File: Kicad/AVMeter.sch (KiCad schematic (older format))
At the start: 62 parts, among them J1 Conn_01x16, J2 Screw_Terminal_01x02, J3 Screw_Terminal_01x02, J4 Screw_Terminal_01x02, J5 Screw_Terminal_01x02, J6 Conn_02x03_Odd_Even, J7 Conn_01x02, J8 Conn_01x02, U1 LT6105, U2 LT6105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

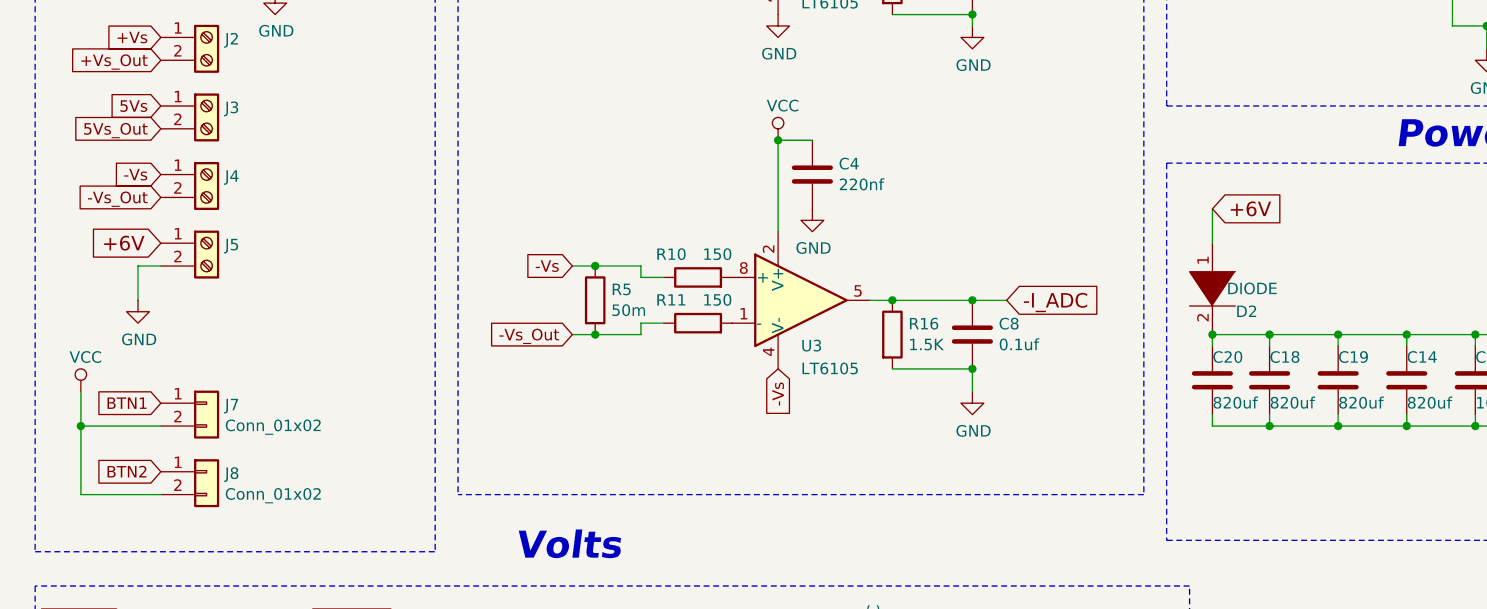
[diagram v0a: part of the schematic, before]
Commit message: fix for LM6105
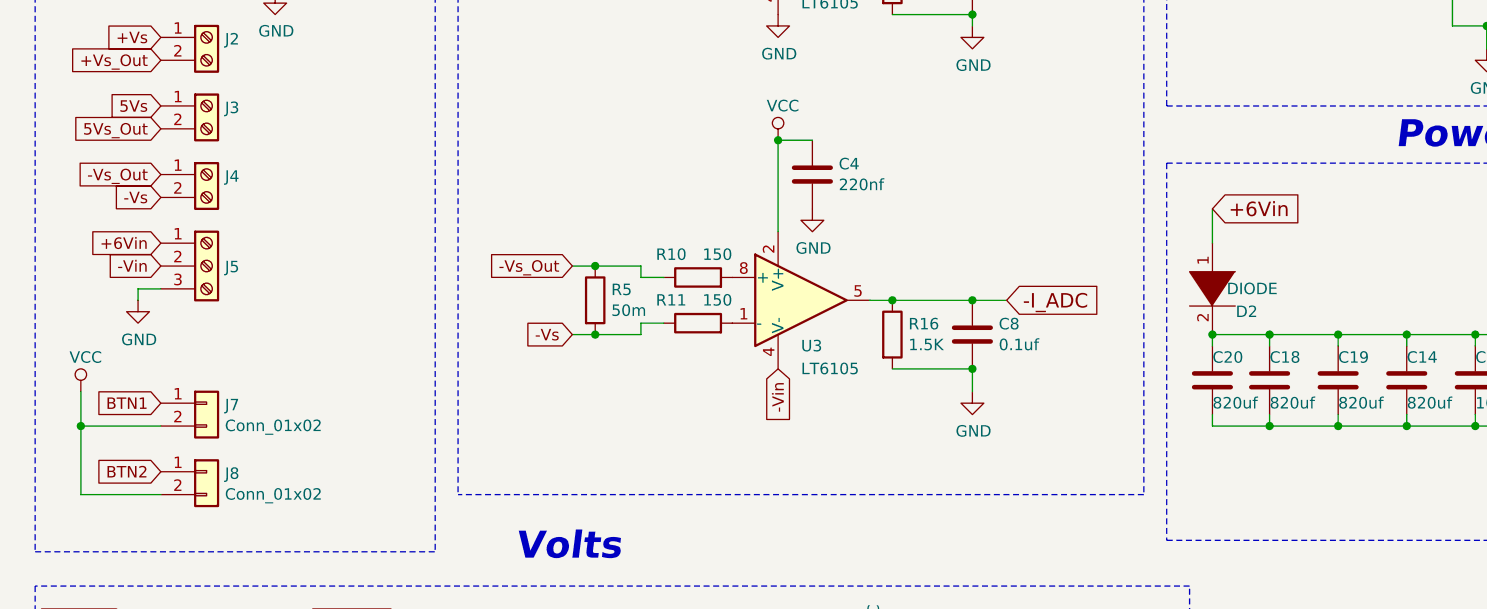
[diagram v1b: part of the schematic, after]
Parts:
- removed J5: Screw_Terminal_01x02, AVMeter:KF301_2Pin_5Pitch, symbol Connector:Screw_Terminal_01x02
- added J5: Screw_Terminal_01x03, AVMeter:KF301_3Pin_5Pitch, symbol Connector:Screw_Terminal_01x03
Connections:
- net -Vs: now also J4.2 (Pin_2), R11.1, R5.2; no longer J4.1 (Pin_1), R10.1, R5.1, U3.4 (V-)
- net -Vs_Out: now also J4.1 (Pin_1), R10.1, R5.1; no longer J4.2 (Pin_2), R11.1, R5.2
- net GND: now also J5.3 (Pin_3)
- net +6V renamed +6Vin
- net +6Vin: now also J5.1 (Pin_1)
- new net -Vin: J5.2 (Pin_2), U3.4 (V-)
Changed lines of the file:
@@
 Text GLabel 1200 4050 0    50   Input ~ 0
 5Vs
-Text GLabel 1200 4350 0    50   Input ~ 0
+Text GLabel 1200 4450 0    50   Input ~ 0
 -Vs
 Text GLabel 1200 3850 0    50   Input ~ 0
@@
 Text GLabel 1200 4150 0    50   Input ~ 0
 5Vs_Out
-Text GLabel 1200 4450 0    50   Input ~ 0
+Text GLabel 1200 4350 0    50   Input ~ 0
 -Vs_Out
 $Comp
@@
 $EndComp
 Text GLabel 3900 5200 3    50   Input ~ 0
--Vs
+-Vin
 $Comp
 L power:VCC #PWR025
@@
 $EndComp
 Text GLabel 5800 4500 2    63   Input ~ 0
-+6V
++6Vin
 $Comp
 L power:GND #PWR036
@@
 Text GLabel 3000 3200 0    50   Input ~ 0
 5Vs
-Text GLabel 3000 4750 0    50   Input ~ 0
+Text GLabel 3000 5050 0    50   Input ~ 0
 -Vs
 Text GLabel 3000 1950 0    50   Input ~ 0
@@
 Text GLabel 3000 3500 0    50   Input ~ 0
 5Vs_Out
-Text GLabel 3000 5050 0    50   Input ~ 0
+Text GLabel 3000 4750 0    50   Input ~ 0
 -Vs_Out
 $Comp
@@
 	1    0    0    -1
 $EndComp
-Text GLabel 1200 4650 0    63   Input ~ 0
-+6V
-Wire Wire Line
-	1200 4750 1100 4750
-Wire Wire Line
-	1100 4750 1100 4900
-$Comp
-L Connector:Screw_Terminal_01x02 J5
-U 1 1 5BCC3B63
-P 1400 4650
-F 0 "J5" H 1480 4642 50  0000 L CNN
-F 1 "Screw_Terminal_01x02" H 1480 4551 50  0001 L CNN
-F 2 "AVMeter:KF301_2Pin_5Pitch" H 1400 4650 50  0001 C CNN
-F 3 "~" H 1400 4650 50  0001 C CNN
-	1    1400 4650
-	1    0    0    -1
-$EndComp
+Text GLabel 1200 4650 0    50   Input ~ 0
++6Vin
+Wire Wire Line
+	1200 4850 1100 4850
+Wire Wire Line
+	1100 4850 1100 4900
 $Comp
 L pspice:DIODE D2
@@
 Wire Wire Line
 	6950 5450 7400 5450
+Text GLabel 1200 4750 0    50   Input ~ 0
+-Vin
+$Comp
+L Connector:Screw_Terminal_01x03 J5
+U 1 1 5D5220A3
+P 1400 4750
+F 0 "J5" H 1480 4746 50  0000 L CNN
+F 1 "Screw_Terminal_01x03" H 1480 4701 50  0001 L CNN
+F 2 "AVMeter:KF301_3Pin_5Pitch" H 1400 4750 50  0001 C CNN
+F 3 "~" H 1400 4750 50  0001 C CNN
+	1    1400 4750
+	1    0    0    -1
+$EndComp
 $EndSCHEMATC

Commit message: added mount holes and other
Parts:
- added C?: 220nf, Capacitor_SMD:C_1206_3216Metric_Pad1.42x1.75mm_HandSolder, symbol AVMeter-rescue:C-Device
- C1, C10, C11, C12, C13, C14, C15, C16, C17, C18, C19, C2, C20, C3, C4, C5, C6, C7, C8, C9: symbol Device:C -> AVMeter-rescue:C-Device
- D1: symbol Reference_Voltage:LM4040DBZ-2.0 -> AVMeter-rescue:LM4040DBZ-2.0-Reference_Voltage
- D2: symbol pspice:DIODE -> AVMeter-rescue:DIODE-pspice
- J1: symbol Connector_Generic:Conn_01x16 -> AVMeter-rescue:Conn_01x16-Connector_Generic
- J2, J3, J4: symbol Connector:Screw_Terminal_01x02 -> AVMeter-rescue:Screw_Terminal_01x02-Connector
- J5: symbol Connector:Screw_Terminal_01x03 -> AVMeter-rescue:Screw_Terminal_01x03-Connector
- J6: symbol Connector_Generic:Conn_02x03_Odd_Even -> AVMeter-rescue:Conn_02x03_Odd_Even-Connector_Generic
- J7, J8: symbol Connector_Generic:Conn_01x02 -> AVMeter-rescue:Conn_01x02-Connector_Generic
- R1, R10, R11, R12, R13, R14, R15, R16, R19, R2, R20, R21, R22, R23, R24, R25, R26, R3, R4, R5, R6, R7, R8, R9: symbol Device:R -> AVMeter-rescue:R-Device
- RV1: symbol Device:R_POT_TRIM -> AVMeter-rescue:R_POT_TRIM-Device
- U4: symbol Amplifier_Operational:LM321 -> AVMeter-rescue:LM321-Amplifier_Operational
- U5: symbol Analog_ADC:MCP3208 -> AVMeter-rescue:MCP3208-Analog_ADC
- U7: symbol Regulator_Linear:L7805 -> AVMeter-rescue:L7805-Regulator_Linear
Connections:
- net -Vin: now also C?.1
- net GND: now also C?.2

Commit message: updated sheet info
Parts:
- gave numbers to parts that had none: 1
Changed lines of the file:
@@
 Sheet 1 1
 Title "AVMeter"
-Date ""
-Rev "1.0"
+Date "2019-08-11"
+Rev "1.2"
 Comp ""
-Comment1 ""
+Comment1 "Fixes both issues found in revisions 1.0 and 1.1"
 Comment2 ""
 Comment3 ""
@@
 $EndComp
 $Comp
-L AVMeter-rescue:C-Device C?
+L AVMeter-rescue:C-Device C21
 U 1 1 5D510CE0
 P 4050 5350
-F 0 "C?" H 4165 5396 50  0000 L CNN
+F 0 "C21" H 4165 5396 50  0000 L CNN
 F 1 "220nf" H 4165 5305 50  0000 L CNN
 F 2 "Capacitor_SMD:C_1206_3216Metric_Pad1.42x1.75mm_HandSolder" H 4088 5200 50  0001 C CNN
@@
 $EndComp
 $Comp
-L AVMeter-rescue:GND-power #PWR?
+L AVMeter-rescue:GND-power #PWR0104
 U 1 1 5D511CD9
 P 4050 5500
-F 0 "#PWR?" H 4050 5250 50  0001 C CNN
+F 0 "#PWR0104" H 4050 5250 50  0001 C CNN
 F 1 "GND" H 4055 5327 50  0000 C CNN
 F 2 "" H 4050 5500 50  0001 C CNN
